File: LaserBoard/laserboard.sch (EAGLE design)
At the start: 22 parts, among them J1 PJ-002AH-SMT-TR, Q1 BSS138, X1 22-23-2021, X2 22-23-2021

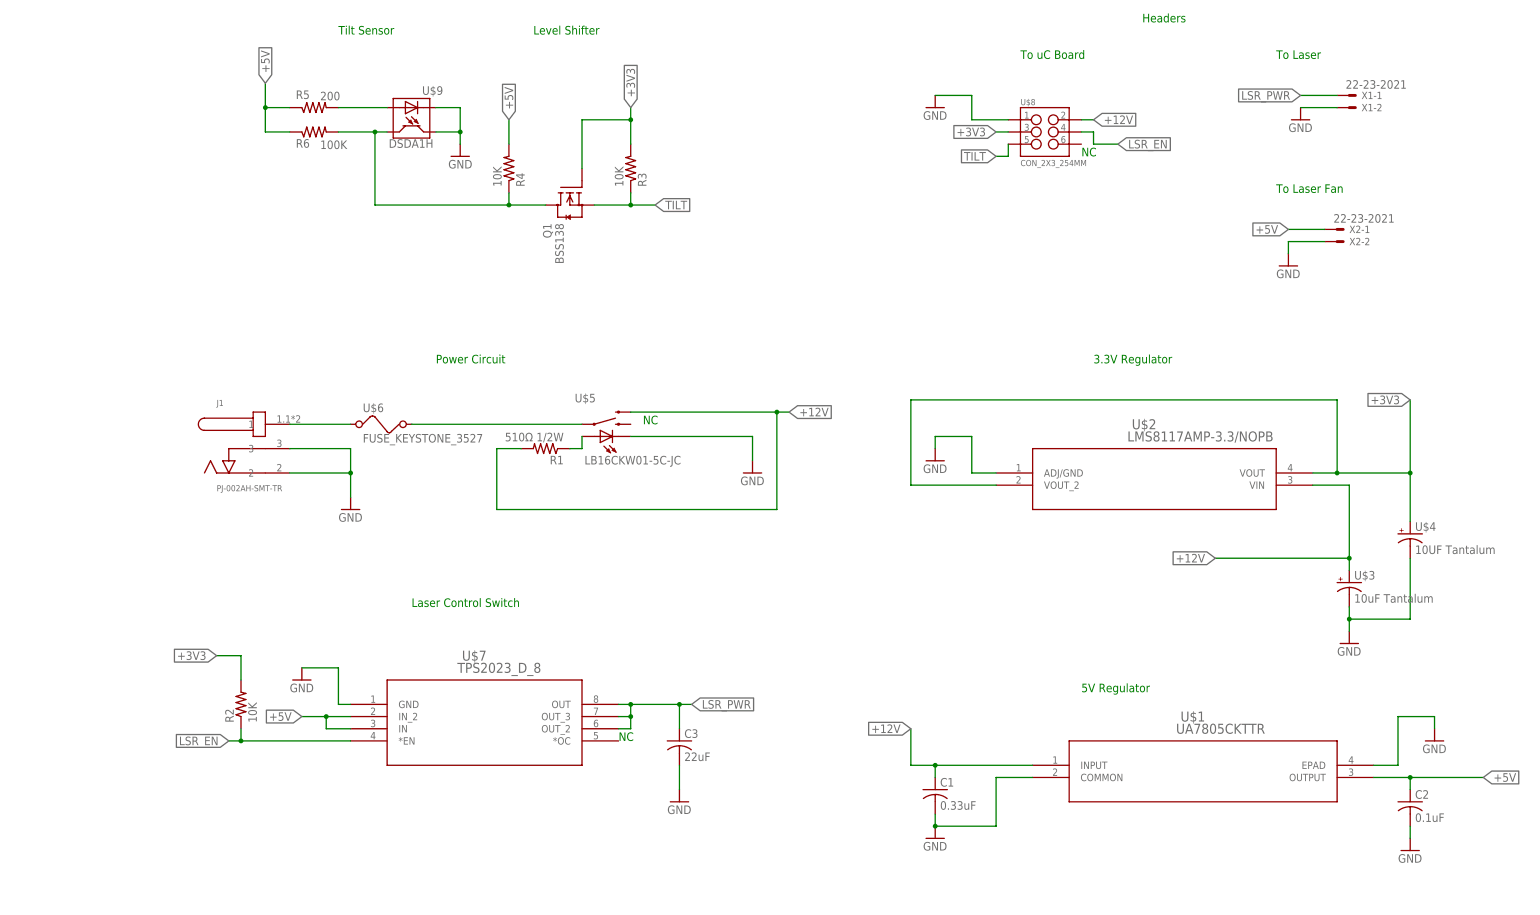
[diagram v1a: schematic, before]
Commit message: Completed Layout of the Laser PCB
This is the completed layout of the Laser PCB. All components and traces
have been laid. The final DRC before manufacturing has not been
performed.
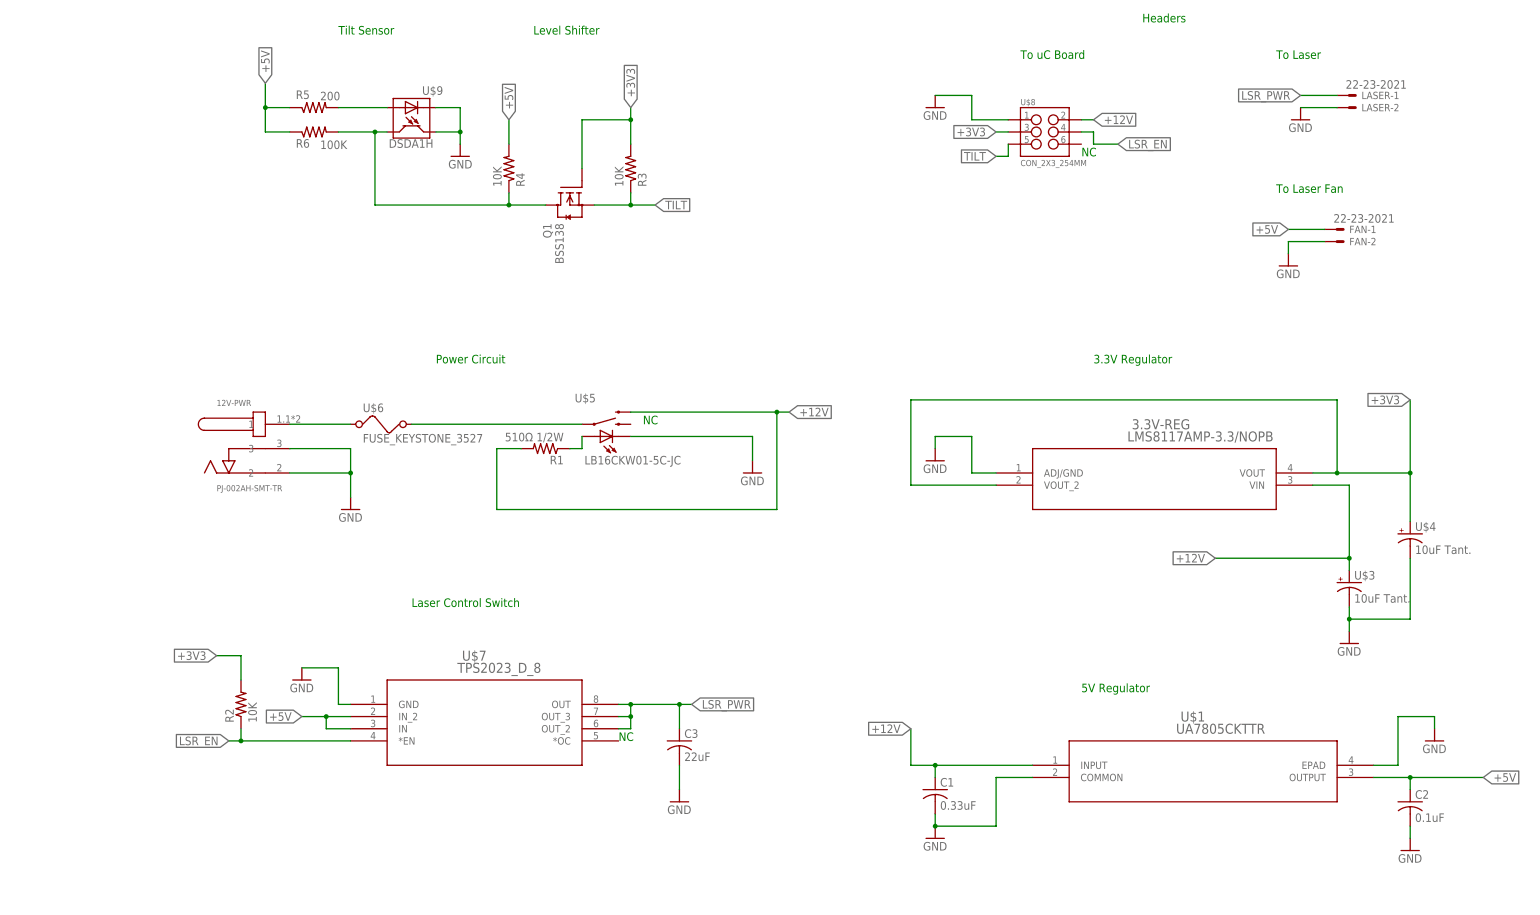
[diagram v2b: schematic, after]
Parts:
- U$3: value 10uF Tantalum -> 10uF Tant.
- U$4: value 10UF Tantalum -> 10uF Tant.
- renumbered J1 to 12V-PWR, U$2 to 3.3V-REG, X1 to LASER, X2 to FAN
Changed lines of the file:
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@@
 <class number="0" name="default" width="0" drill="0">
+</class>
+<class number="1" name="Laser 5v" width="0" drill="0">
 </class>
 </classes>
@@
 <part name="GND2" library="supply1" deviceset="GND" device=""/>
 <part name="GND3" library="supply1" deviceset="GND" device=""/>
-<part name="U$2" library="LMS8117AMP-3_3NOPB" deviceset="LMS8117AMP-3.3/NOPB" device=""/>
+<part name="3.3V-REG" library="LMS8117AMP-3_3NOPB" deviceset="LMS8117AMP-3.3/NOPB" device=""/>
 <part name="C1" library="rcl" deviceset="C-US" device="C0805" value="0.33uF"/>
 <part name="C2" library="rcl" deviceset="C-US" device="C0805" value="0.1uF"/>
 <part name="GND4" library="supply1" deviceset="GND" device=""/>
 <part name="GND5" library="supply1" deviceset="GND" device=""/>
-<part name="J1" library="PJ-002AH-SMT-TR" deviceset="PJ-002AH-SMT-TR" device=""/>
+<part name="12V-PWR" library="PJ-002AH-SMT-TR" deviceset="PJ-002AH-SMT-TR" device=""/>
 <part name="GND6" library="supply1" deviceset="GND" device=""/>
-<part name="U$3" library="ChristiansCustom" deviceset="CAPACITOR_POL_0805" device="" value="10uF Tantalum"/>
-<part name="U$4" library="ChristiansCustom" deviceset="CAPACITOR_POL_0805" device="" value="10UF Tantalum"/>
+<part name="U$3" library="ChristiansCustom" deviceset="CAPACITOR_POL_0805" device="" value="10uF Tant."/>
+<part name="U$4" library="ChristiansCustom" deviceset="CAPACITOR_POL_0805" device="" value="10uF Tant."/>
 <part name="U$5" library="ChristiansCustom" deviceset="LB16CKW01-5C-JC" device=""/>
 <part name="GND7" library="supply1" deviceset="GND" device=""/>
@@
 <part name="GND9" library="supply1" deviceset="GND" device=""/>
 <part name="R2" library="rcl" deviceset="R-US_" device="R0805" value="10K"/>
-<part name="X1" library="con-molex" deviceset="22-23-2021" device=""/>
-<part name="X2" library="con-molex" deviceset="22-23-2021" device=""/>
+<part name="LASER" library="con-molex" deviceset="22-23-2021" device=""/>
+<part name="FAN" library="con-molex" deviceset="22-23-2021" device=""/>
 <part name="GND10" library="supply1" deviceset="GND" device=""/>
 <part name="GND11" library="supply1" deviceset="GND" device=""/>
@@
 <instance part="GND2" gate="1" x="215.9" y="45.72"/>
 <instance part="GND3" gate="1" x="314.96" y="43.18"/>
-<instance part="U$2" gate="A" x="228.6" y="121.92"/>
+<instance part="3.3V-REG" gate="A" x="228.6" y="121.92"/>
 <instance part="C1" gate="G$1" x="215.9" y="55.88"/>
 <instance part="C2" gate="G$1" x="314.96" y="53.34"/>
 <instance part="GND4" gate="1" x="215.9" y="124.46"/>
 <instance part="GND5" gate="1" x="302.26" y="86.36"/>
-<instance part="J1" gate="G$1" x="76.2" y="127"/>
+<instance part="12V-PWR" gate="G$1" x="76.2" y="127"/>
 <instance part="GND6" gate="1" x="93.98" y="114.3"/>
 <instance part="U$3" gate="G$1" x="302.26" y="99.06"/>
@@
 <instance part="GND9" gate="1" x="162.56" y="53.34"/>
 <instance part="R2" gate="G$1" x="71.12" y="73.66" rot="R90"/>
-<instance part="X1" gate="-1" x="302.26" y="200.66"/>
-<instance part="X1" gate="-2" x="302.26" y="198.12"/>
-<instance part="X2" gate="-1" x="299.72" y="172.72"/>
-<instance part="X2" gate="-2" x="299.72" y="170.18"/>
+<instance part="LASER" gate="-1" x="302.26" y="200.66"/>
+<instance part="LASER" gate="-2" x="302.26" y="198.12"/>
+<instance part="FAN" gate="-1" x="299.72" y="172.72"/>
+<instance part="FAN" gate="-2" x="299.72" y="170.18"/>
 <instance part="GND10" gate="1" x="292.1" y="195.58"/>
 <instance part="GND11" gate="1" x="289.56" y="165.1"/>
@@
 </segment>
 <segment>
-<pinref part="U$2" gate="A" pin="ADJ/GND"/>
+<pinref part="3.3V-REG" gate="A" pin="ADJ/GND"/>
 <wire x1="228.6" y1="121.92" x2="223.52" y2="121.92" width="0.1524" layer="91"/>
 <wire x1="223.52" y1="121.92" x2="223.52" y2="129.54" width="0.1524" layer="91"/>
@@
 </segment>
 <segment>
-<pinref part="J1" gate="G$1" pin="3"/>
+<pinref part="12V-PWR" gate="G$1" pin="3"/>
 <pinref part="GND6" gate="1" pin="GND"/>
 <wire x1="81.28" y1="127" x2="93.98" y2="127" width="0.1524" layer="91"/>
 <wire x1="93.98" y1="127" x2="93.98" y2="121.92" width="0.1524" layer="91"/>
-<pinref part="J1" gate="G$1" pin="2"/>
+<pinref part="12V-PWR" gate="G$1" pin="2"/>
 <wire x1="93.98" y1="121.92" x2="93.98" y2="116.84" width="0.1524" layer="91"/>
 <wire x1="81.28" y1="121.92" x2="93.98" y2="121.92" width="0.1524" layer="91"/>
@@
 </segment>
 <segment>
-<pinref part="X1" gate="-2" pin="S"/>
+<pinref part="LASER" gate="-2" pin="S"/>
 <pinref part="GND10" gate="1" pin="GND"/>
 <wire x1="299.72" y1="198.12" x2="292.1" y2="198.12" width="0.1524" layer="91"/>
 </segment>
 <segment>
-<pinref part="X2" gate="-2" pin="S"/>
+<pinref part="FAN" gate="-2" pin="S"/>
 <pinref part="GND11" gate="1" pin="GND"/>
 <wire x1="297.18" y1="170.18" x2="289.56" y2="170.18" width="0.1524" layer="91"/>
@@
 <wire x1="314.96" y1="121.92" x2="314.96" y2="137.16" width="0.1524" layer="91"/>
 <junction x="314.96" y="121.92"/>
-<pinref part="U$2" gate="A" pin="VOUT_2"/>
+<pinref part="3.3V-REG" gate="A" pin="VOUT_2"/>
 <wire x1="228.6" y1="119.38" x2="210.82" y2="119.38" width="0.1524" layer="91"/>
-<pinref part="U$2" gate="A" pin="VOUT"/>
+<pinref part="3.3V-REG" gate="A" pin="VOUT"/>
 <wire x1="294.64" y1="121.92" x2="299.72" y2="121.92" width="0.1524" layer="91"/>
 <junction x="299.72" y="121.92"/>
@@
 </segment>
 </net>
-<net name="+5V" class="0">
+<net name="+5V" class="1">
 <segment>
 <wire x1="314.96" y1="55.88" x2="314.96" y2="58.42" width="0.1524" layer="91"/>
@@
 </segment>
 <segment>
-<pinref part="X2" gate="-1" pin="S"/>
+<pinref part="FAN" gate="-1" pin="S"/>
 <wire x1="297.18" y1="172.72" x2="289.56" y2="172.72" width="0.1524" layer="91"/>
 <label x="289.56" y="172.72" size="1.778" layer="95" rot="R180" xref="yes"/>
@@
 <wire x1="302.26" y1="119.38" x2="302.26" y2="104.14" width="0.1524" layer="91"/>
 <junction x="302.26" y="104.14"/>
-<pinref part="U$2" gate="A" pin="VIN"/>
+<pinref part="3.3V-REG" gate="A" pin="VIN"/>
 <wire x1="294.64" y1="119.38" x2="302.26" y2="119.38" width="0.1524" layer="91"/>
 <label x="274.32" y="104.14" size="1.778" layer="95" rot="R180" xref="yes"/>
@@
 <net name="N$2" class="0">
 <segment>
-<pinref part="J1" gate="G$1" pin="1"/>
+<pinref part="12V-PWR" gate="G$1" pin="1"/>
 <pinref part="U$6" gate="G$1" pin="1"/>
 <wire x1="81.28" y1="132.08" x2="93.98" y2="132.08" width="0.1524" layer="91"/>
@@
 </segment>
 </net>
-<net name="LSR_PWR" class="0">
+<net name="LSR_PWR" class="1">
 <segment>
 <pinref part="U$7" gate="A" pin="OUT_2"/>
@@
 </segment>
 <segment>
-<pinref part="X1" gate="-1" pin="S"/>
+<pinref part="LASER" gate="-1" pin="S"/>
 <wire x1="299.72" y1="200.66" x2="292.1" y2="200.66" width="0.1524" layer="91"/>
 <label x="292.1" y="200.66" size="1.778" layer="95" rot="R180" xref="yes"/>

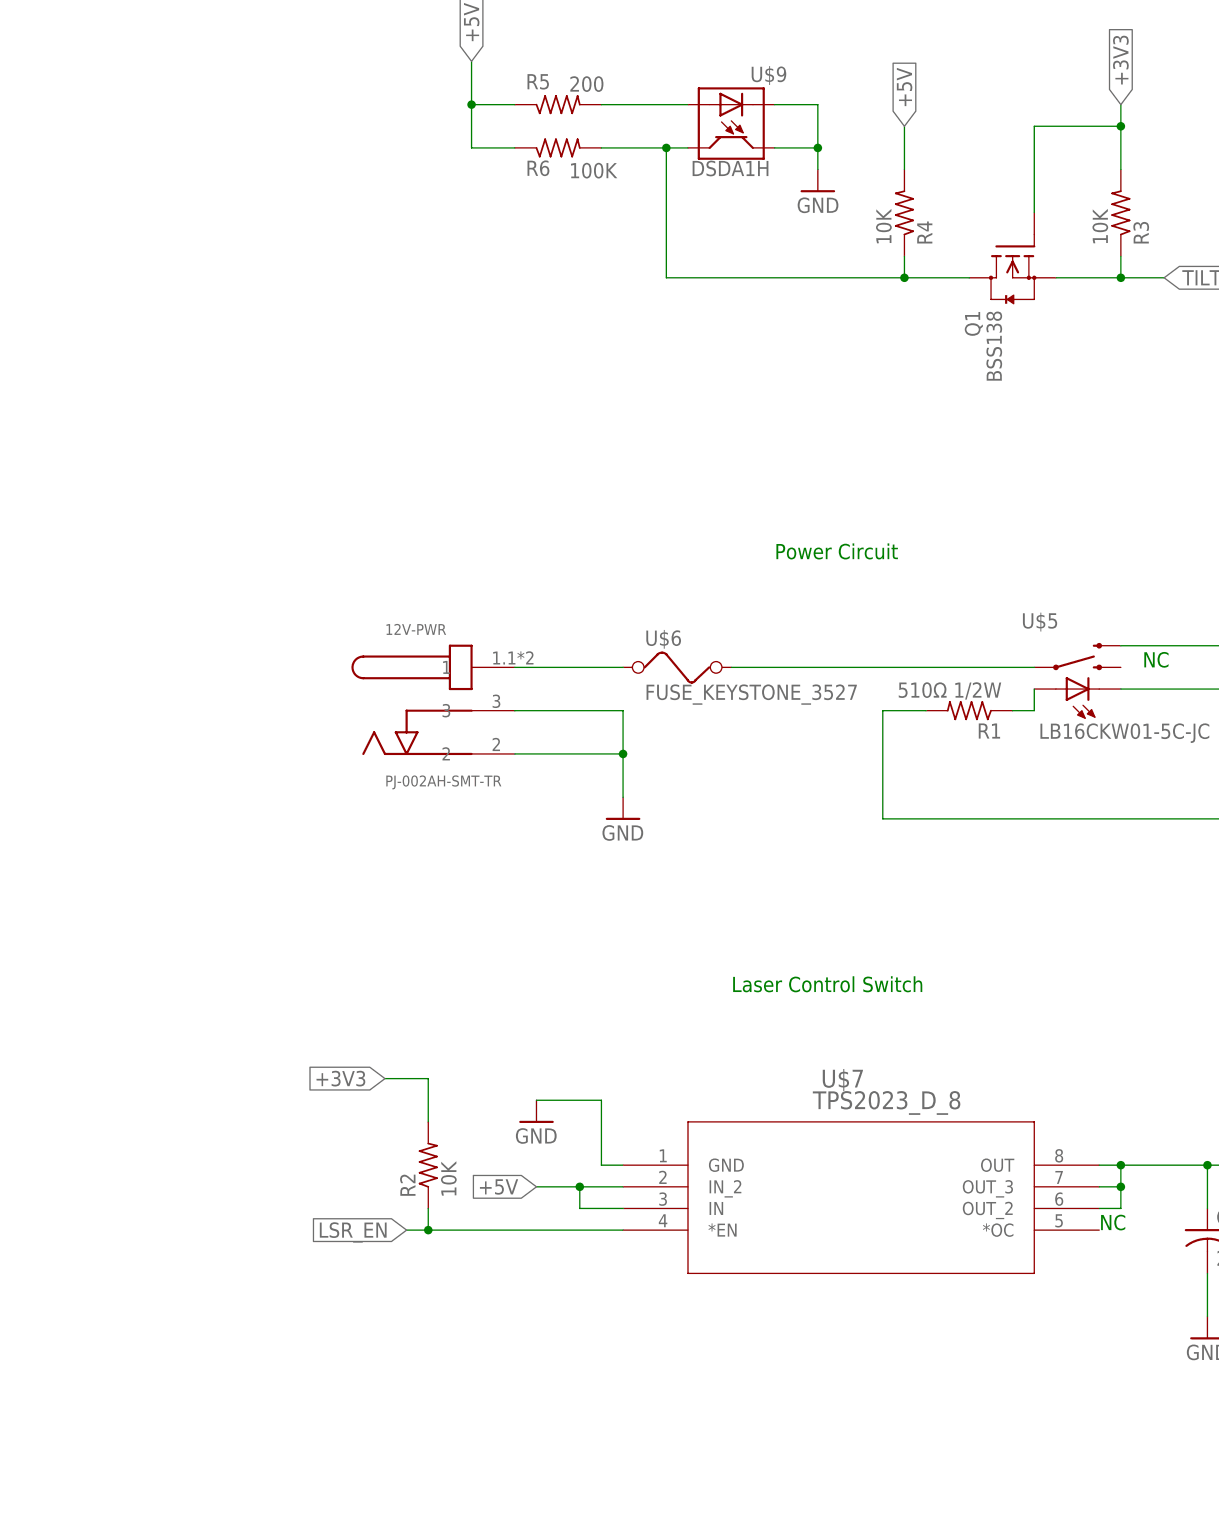
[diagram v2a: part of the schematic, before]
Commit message: Fixing schematics for design review, adding block diagram, upgrading version to prototype version 2
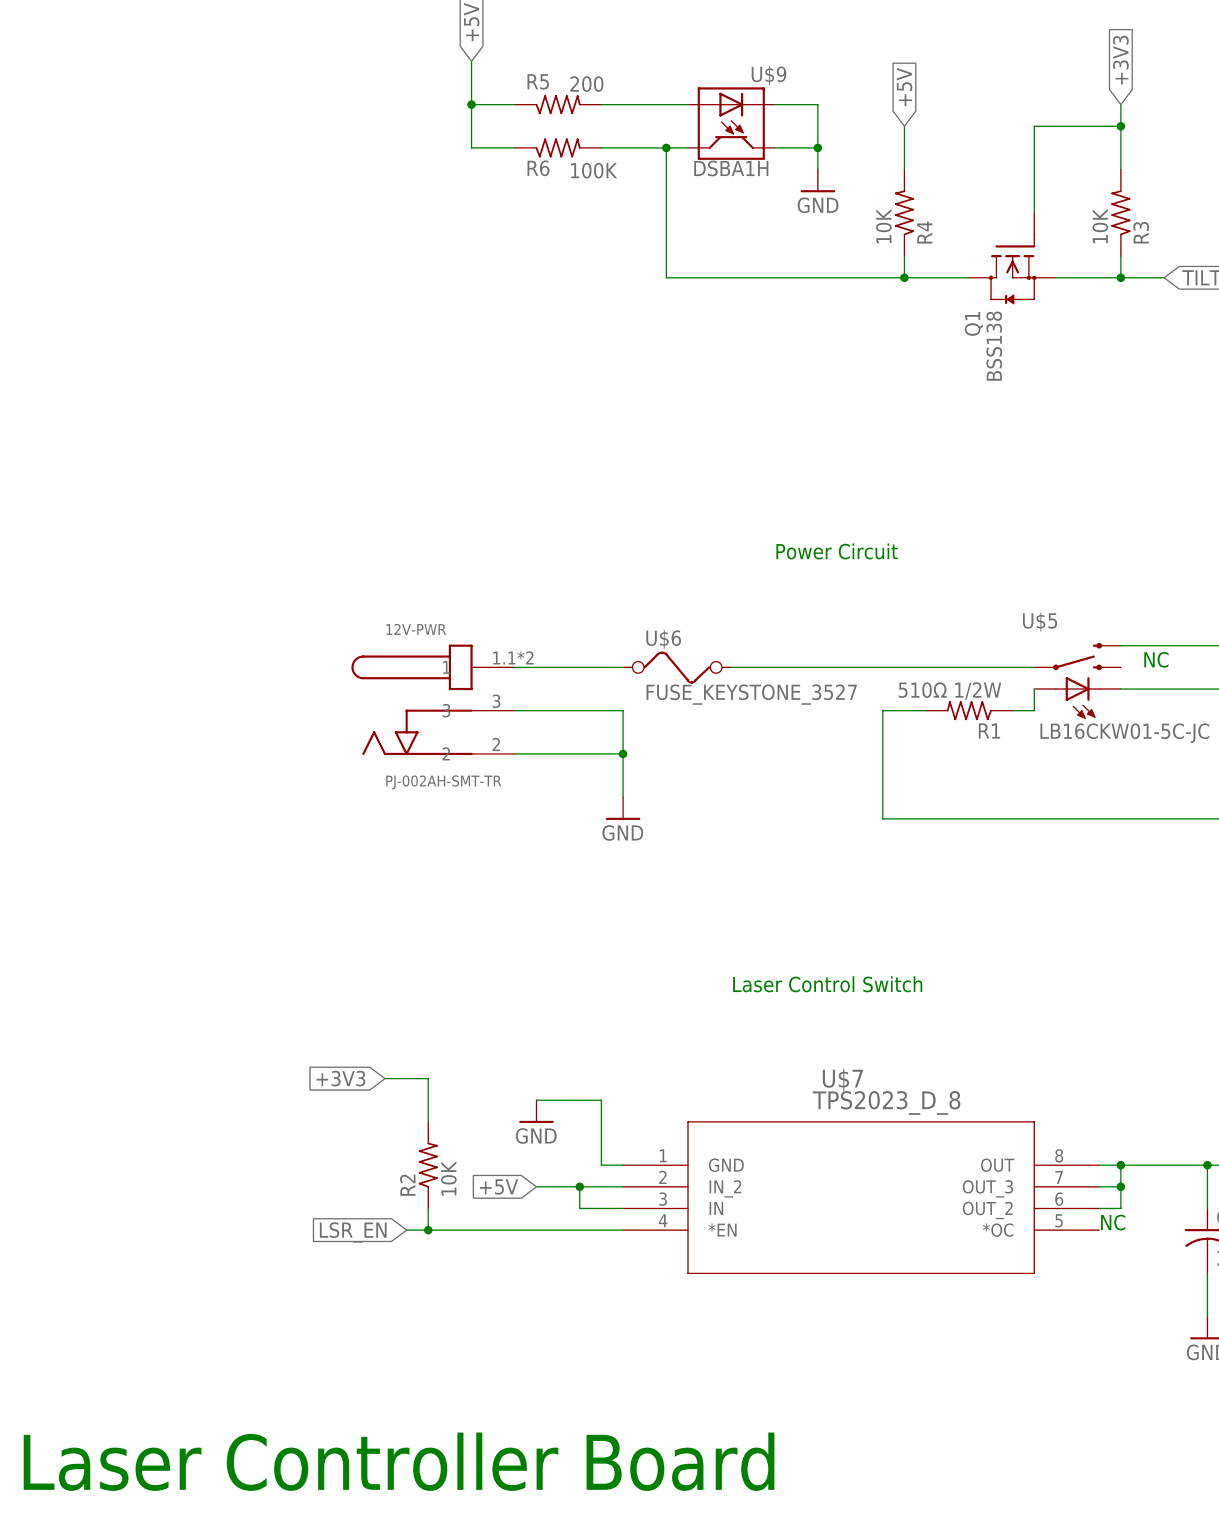
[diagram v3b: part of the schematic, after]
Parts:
- U$9: value DSDA1H -> DSBA1H; device ChristiansCustom:DSDA1H -> ChristiansCustom:DSBA1H
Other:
- note added: "Laser Controller Board"
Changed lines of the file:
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@@
 <part name="R3" library="rcl" deviceset="R-US_" device="R0805" value="10K"/>
 <part name="R4" library="rcl" deviceset="R-US_" device="R0805" value="10K"/>
-<part name="U$9" library="ChristiansCustom" deviceset="DSDA1H" device=""/>
+<part name="U$9" library="ChristiansCustom" deviceset="DSBA1H" device=""/>
 <part name="R5" library="rcl" deviceset="R-US_" device="R0805" value="200"/>
 <part name="R6" library="rcl" deviceset="R-US_" device="R0805" value="100K"/>
@@
 <text x="91.44" y="213.36" size="1.778" layer="91">Tilt Sensor</text>
 <text x="132.08" y="213.36" size="1.778" layer="91">Level Shifter</text>
+<text x="22.86" y="35.56" size="6.4516" layer="91">Laser Controller Board</text>
 </plain>
 <instances>
